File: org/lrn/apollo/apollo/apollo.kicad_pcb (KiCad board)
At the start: 2 copper layers, 47 parts, among them J1 Conn_01x01_Male, J2 Conn_01x01_Male, J3 Conn_01x01_Male, J4 Conn_01x01_Male, Q1 PN2222A, Q2 PN2222A, Q3 PN2222A, Q4 PN2222A, U1 74HC595, U2 5461AS-1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

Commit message: apollo: keyb dbg wip
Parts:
- removed the J1 at (95.0, 106.2)
- removed the J1 at (95.1, 122.2)
- removed the J1 at (90.6, 106.2)
- removed the J1 at (110.9, 103.9)
- moved JA_15 95.9 mm to (111.8, 30.1), turned to 0 degrees
- moved JDS_14 94.8 mm to (141.0, 38.2), turned to 270 degrees
- moved U3 91.8 mm to (119.4, 32.6), turned to 0 degrees
- moved JB_1 91.0 mm to (111.8, 32.6), turned to 0 degrees
- moved JC_2 85.9 mm to (111.8, 35.1), turned to 0 degrees
- moved JST_CP_RCLK_12 85.8 mm to (141.0, 44.0), turned to 0 degrees
- moved JD_3 80.8 mm to (111.8, 37.7), turned to 0 degrees
- moved JSH_CP_SRCLK_11 79.2 mm to (141.0, 49.8), turned to 0 degrees
- moved JE_4 75.7 mm to (111.8, 40.2), turned to 0 degrees
- moved JF_5 70.7 mm to (111.8, 42.7), turned to 0 degrees
- moved JG_6 65.6 mm to (111.8, 45.3), turned to 0 degrees
- moved JH_7 60.5 mm to (111.8, 47.8), turned to 0 degrees
- moved J1 56.1 mm to (183.7, 55.6)
- moved J2 56.1 mm to (166.3, 55.6)
- moved J3 56.1 mm to (172.1, 55.6)
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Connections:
- U4 pad 14: Net-(U4-Pad14) -> Net-(JST_CP_RCLK_12-Pad1)
- U4 pad 15: Net-(U4-Pad15) -> Net-(JSH_CP_SRCLK_11-Pad1)
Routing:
- net Net-(JSH_CP_SRCLK_11-Pad1): track 8.64 -> 21.9 mm
- net Net-(JST_CP_RCLK_12-Pad1): track 8.66 -> 21.8 mm
- net VCC: track 56.8 -> 52.8 mm

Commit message: apollo: pcb additions
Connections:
- U4 pad 13: Net-(U4-Pad13) -> Net-(JDS_14-Pad1)
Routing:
- net Net-(JDS_14-Pad1): track 8.59 -> 26.6 mm
- net GND: track 248.6 -> 243.8 mm
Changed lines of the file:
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@@
     (thickness 1.6)
     (drawings 0)
-    (tracks 254)
+    (tracks 259)
     (zones 0)
     (modules 43)
-    (nets 63)
+    (nets 62)
   )
   (page A4)
@@
   (net 50 "Net-(U4-Pad12)")
   (net 51 "Net-(U4-Pad3)")
-  (net 52 "Net-(U4-Pad13)")
-  (net 53 "Net-(U4-Pad4)")
-  (net 54 "Net-(U4-Pad5)")
-  (net 55 "Net-(U4-Pad6)")
-  (net 56 "Net-(U4-Pad9)")
-  (net 57 "Net-(U4-Pad10)")
-  (net 58 "Net-(U4-Pad20)")
-  (net 59 "Net-(U4-Pad21)")
-  (net 60 "Net-(J_MOSI_1-Pad1)")
-  (net 61 "Net-(J_MISO_1-Pad1)")
-  (net 62 "Net-(J_SCK_1-Pad1)")
+  (net 52 "Net-(U4-Pad4)")
+  (net 53 "Net-(U4-Pad5)")
+  (net 54 "Net-(U4-Pad6)")
+  (net 55 "Net-(U4-Pad9)")
+  (net 56 "Net-(U4-Pad10)")
+  (net 57 "Net-(U4-Pad20)")
+  (net 58 "Net-(U4-Pad21)")
+  (net 59 "Net-(J_MOSI_1-Pad1)")
+  (net 60 "Net-(J_MISO_1-Pad1)")
+  (net 61 "Net-(J_SCK_1-Pad1)")
   (net_class Default "This is the default net class."
     (clearance 0.8)
@@
     (add_net "Net-(U4-Pad11)")
     (add_net "Net-(U4-Pad12)")
-    (add_net "Net-(U4-Pad13)")
     (add_net "Net-(U4-Pad2)")
     (add_net "Net-(U4-Pad20)")
@@
       (net 51 "Net-(U4-Pad3)"))
     (pad 17 thru_hole oval (at 7.62 27.94 270) (size 3 1.6) (drill 0.8) (layers *.Cu *.Mask)
-      (net 60 "Net-(J_MOSI_1-Pad1)"))
+      (net 59 "Net-(J_MOSI_1-Pad1)"))
     (pad 4 thru_hole oval (at 0 7.62 270) (size 3 1.6) (drill 0.8) (layers *.Cu *.Mask)
-      (net 53 "Net-(U4-Pad4)"))
+      (net 52 "Net-(U4-Pad4)"))
     (pad 18 thru_hole oval (at 7.62 25.4 270) (size 3 1.6) (drill 0.8) (layers *.Cu *.Mask)
-      (net 61 "Net-(J_MISO_1-Pad1)"))
+      (net 60 "Net-(J_MISO_1-Pad1)"))
     (pad 5 thru_hole oval (at 0 10.16 270) (size 3 1.6) (drill 0.8) (layers *.Cu *.Mask)
-      (net 54 "Net-(U4-Pad5)"))
+      (net 53 "Net-(U4-Pad5)"))
     (pad 19 thru_hole oval (at 7.62 22.86 270) (size 3 1.6) (drill 0.8) (layers *.Cu *.Mask)
-      (net 62 "Net-(J_SCK_1-Pad1)"))
+      (net 61 "Net-(J_SCK_1-Pad1)"))
     (pad 6 thru_hole oval (at 0 12.7 270) (size 3 1.6) (drill 0.8) (layers *.Cu *.Mask)
-      (net 55 "Net-(U4-Pad6)"))
+      (net 54 "Net-(U4-Pad6)"))
     (pad 20 thru_hole oval (at 7.62 20.32 270) (size 3 1.6) (drill 0.8) (layers *.Cu *.Mask)
-      (net 58 "Net-(U4-Pad20)"))
+      (net 57 "Net-(U4-Pad20)"))
     (pad 7 thru_hole oval (at 0 15.24 270) (size 3 1.6) (drill 0.8) (layers *.Cu *.Mask)
       (net 34 VCC))
     (pad 21 thru_hole oval (at 7.62 17.78 270) (size 3 1.6) (drill 0.8) (layers *.Cu *.Mask)
-      (net 59 "Net-(U4-Pad21)"))
+      (net 58 "Net-(U4-Pad21)"))
     (pad 8 thru_hole oval (at 0 17.78 270) (size 3 1.6) (drill 0.8) (layers *.Cu *.Mask)
       (net 33 GND))
@@
       (net 33 GND))
     (pad 9 thru_hole oval (at 0 20.32 270) (size 3 1.6) (drill 0.8) (layers *.Cu *.Mask)
-      (net 56 "Net-(U4-Pad9)"))
+      (net 55 "Net-(U4-Pad9)"))
     (pad 23 thru_hole oval (at 7.62 12.7 270) (size 3 1.6) (drill 0.8) (layers *.Cu *.Mask)
       (net 3 "Net-(J2-Pad1)"))
     (pad 10 thru_hole oval (at 0 22.86 270) (size 3 1.6) (drill 0.8) (layers *.Cu *.Mask)
-      (net 57 "Net-(U4-Pad10)"))
+      (net 56 "Net-(U4-Pad10)"))
     (pad 24 thru_hole oval (at 7.62 10.16 270) (size 3 1.6) (drill 0.8) (layers *.Cu *.Mask)
       (net 4 "Net-(J3-Pad1)"))
@@
       (net 2 "Net-(J1-Pad1)"))
     (pad 13 thru_hole oval (at 0 30.48 270) (size 3 1.6) (drill 0.8) (layers *.Cu *.Mask)
-      (net 52 "Net-(U4-Pad13)"))
+      (net 39 "Net-(JDS_14-Pad1)"))
     (pad 27 thru_hole oval (at 7.62 2.54 270) (size 3 1.6) (drill 0.8) (layers *.Cu *.Mask)
       (net 8 "Net-(J_SER1-Pad1)"))
@@
     )
     (pad 1 thru_hole oval (at 0 0 90) (size 3 1.6) (drill 0.7) (layers *.Cu *.Mask)
-      (net 61 "Net-(J_MISO_1-Pad1)"))
+      (net 60 "Net-(J_MISO_1-Pad1)"))
     (model ${KISYS3DMOD}/Connector_Pin.3dshapes/Pin_D0.7mm_L6.5mm_W1.8mm_FlatFork.wrl
       (at (xyz 0 0 0))
@@
     (fp_line (start 1.35 1.2) (end -1.4 1.2) (layer F.CrtYd) (width 0.05))
     (pad 1 thru_hole oval (at 0 0 90) (size 3 1.6) (drill 0.7) (layers *.Cu *.Mask)
-      (net 60 "Net-(J_MOSI_1-Pad1)"))
+      (net 59 "Net-(J_MOSI_1-Pad1)"))
     (model ${KISYS3DMOD}/Connector_Pin.3dshapes/Pin_D0.7mm_L6.5mm_W1.8mm_FlatFork.wrl
       (at (xyz 0 0 0))
@@
     (fp_line (start 1.35 1.2) (end -1.4 1.2) (layer F.CrtYd) (width 0.05))
     (pad 1 thru_hole oval (at 0 0 90) (size 3 1.6) (drill 0.7) (layers *.Cu *.Mask)
-      (net 62 "Net-(J_SCK_1-Pad1)"))
+      (net 61 "Net-(J_SCK_1-Pad1)"))
     (model ${KISYS3DMOD}/Connector_Pin.3dshapes/Pin_D0.7mm_L6.5mm_W1.8mm_FlatFork.wrl
       (at (xyz 0 0 0))
@@
   (segment (start 123.33732 49.4792) (end 122.463359 50.353161) (width 1) (layer B.Cu) (net 33))
   (segment (start 119.447841 50.353161) (end 119.447841 50.366399) (width 1) (layer B.Cu) (net 33))
-  (segment (start 119.447841 50.366399) (end 117.71122 52.10302) (width 1) (layer B.Cu) (net 33))
-  (segment (start 117.71122 52.10302) (end 115.33886 52.10302) (width 1) (layer B.Cu) (net 33))
   (segment (start 157.05836 125.0788) (end 139.9632 125.0788) (width 1) (layer B.Cu) (net 33))
   (segment (start 163.8808 71.5518) (end 163.8808 70.231) (width 1) (layer B.Cu) (net 33))
@@
   (segment (start 135.661199 37.653161) (end 135.6614 37.65296) (width 1) (layer B.Cu) (net 39))
   (segment (start 127.067841 37.653161) (end 135.661199 37.653161) (width 1) (layer B.Cu) (net 39))
+  (segment (start 148.5138 36.2604) (end 146.5434 34.29) (width 1) (layer B.Cu) (net 39))
+  (segment (start 148.5138 38.7604) (end 148.5138 36.2604) (width 1) (layer B.Cu) (net 39))
+  (segment (start 144.9264 34.29) (end 141.0208 38.1956) (width 1) (layer B.Cu) (net 39))
+  (segment (start 146.5434 34.29) (end 144.9264 34.29) (width 1) (layer B.Cu) (net 39))
+  (segment (start 135.661199 37.653161) (end 136.651799 37.653161) (width 1) (layer B.Cu) (net 39))
+  (segment (start 137.194238 38.1956) (end 141.0208 38.1956) (width 1) (layer B.Cu) (net 39))
+  (segment (start 136.651799 37.653161) (end 137.194238 38.1956) (width 1) (layer B.Cu) (net 39))
   (segment (start 111.856319 40.193161) (end 111.81588 40.2336) (width 1) (layer B.Cu) (net 40))
   (segment (start 119.447841 40.193161) (end 111.856319 40.193161) (width 1) (layer B.Cu) (net 40))
@@
   (segment (start 141.0208 43.7134) (end 145.9738 38.7604) (width 1) (layer B.Cu) (net 45))
   (segment (start 141.0208 44.0122) (end 141.0208 43.7134) (width 1) (layer B.Cu) (net 45))
-  (segment (start 151.0538 46.3804) (end 151.0538 52.0058) (width 1) (layer B.Cu) (net 60))
-  (segment (start 153.5938 51.9804) (end 153.6192 52.0058) (width 1) (layer B.Cu) (net 61))
-  (segment (start 153.5938 46.3804) (end 153.5938 51.9804) (width 1) (layer B.Cu) (net 61))
-  (segment (start 156.1338 46.3804) (end 156.1338 52.0058) (width 1) (layer B.Cu) (net 62))
+  (segment (start 151.0538 46.3804) (end 151.0538 52.0058) (width 1) (layer B.Cu) (net 59))
+  (segment (start 153.5938 51.9804) (end 153.6192 52.0058) (width 1) (layer B.Cu) (net 60))
+  (segment (start 153.5938 46.3804) (end 153.5938 51.9804) (width 1) (layer B.Cu) (net 60))
+  (segment (start 156.1338 46.3804) (end 156.1338 52.0058) (width 1) (layer B.Cu) (net 61))
 )

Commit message: apollo: before keyb scan
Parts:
- moved JH_7 8.39 mm to (119.3, 51.5)
- moved U3 8.39 mm to (127.0, 36.3)
- moved JA_15 8.39 mm to (119.3, 33.8)
- moved JC_2 8.39 mm to (119.3, 38.8)
- moved JD_3 8.39 mm to (119.3, 41.4)
- moved JF_5 8.39 mm to (119.3, 46.5)
- moved JG_6 8.39 mm to (119.4, 49.0)
- moved JB_1 8.39 mm to (119.3, 36.3)
- moved JE_4 8.39 mm to (119.3, 44.0)
- renumbered J_CLR1 to J_D_CLOCK_1, J_SER1 to J_D_DATA_1, J_CLK1 to J_D_LATCH_1, JSH_CP_SRCLK_11 to J_K_CLOCK_1, JDS_14 to J_K_DATA_1, JST_CP_RCLK_12 to J_K_LATCH_1
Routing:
- net VCC: track 52.8 -> 82.1 mm, vias 2 -> 0
- net Net-(JA_15-Pad1): track 19.2 -> 0.00 mm
- net GND: track 243.8 -> 227.4 mm
- net Net-(J_K_CLOCK_1-Pad1): track 21.9 -> 12.5 mm
- net Net-(J_K_DATA_1-Pad1): track 26.6 -> 18.3 mm
- net Net-(J_K_LATCH_1-Pad1): track 21.8 -> 14.3 mm
- net Net-(J_D_LATCH_1-Pad1): track 153.2 -> 150.7 mm

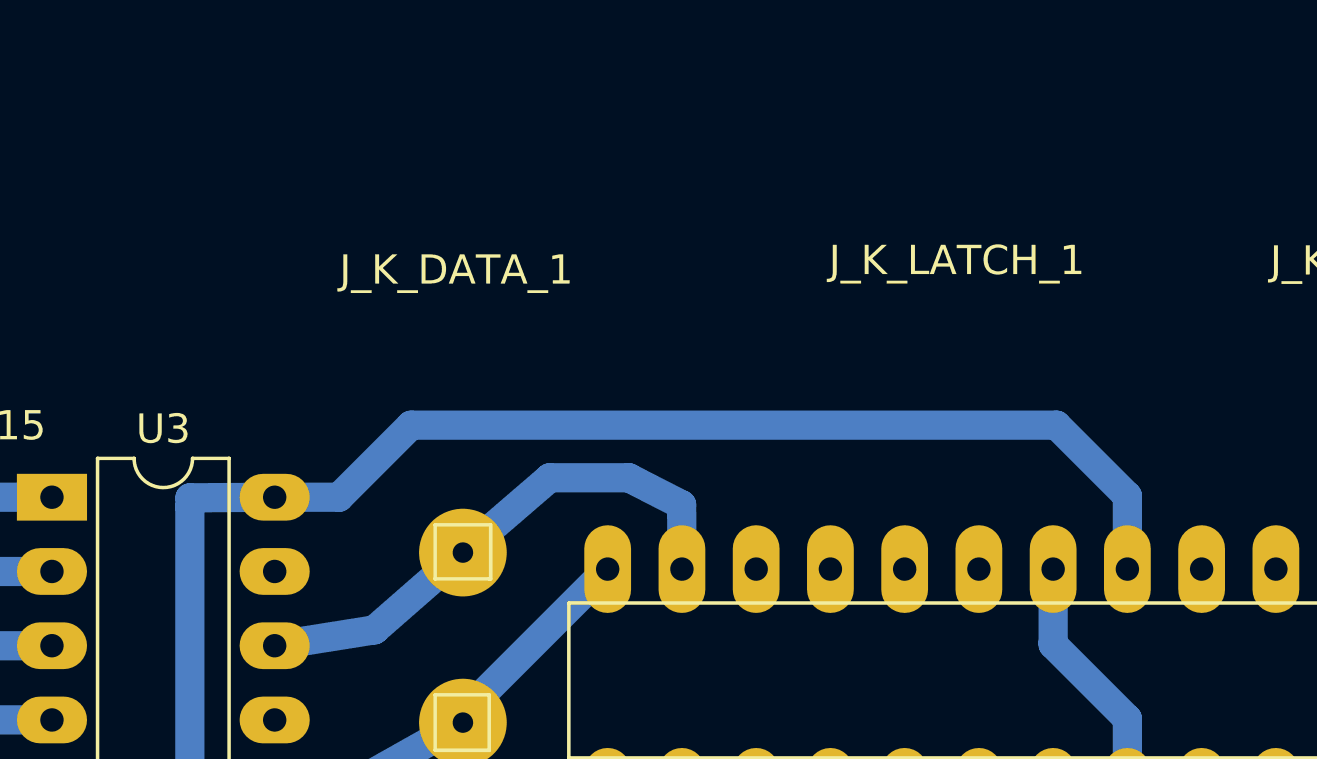
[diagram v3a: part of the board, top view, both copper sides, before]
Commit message: apollo: beep schematic
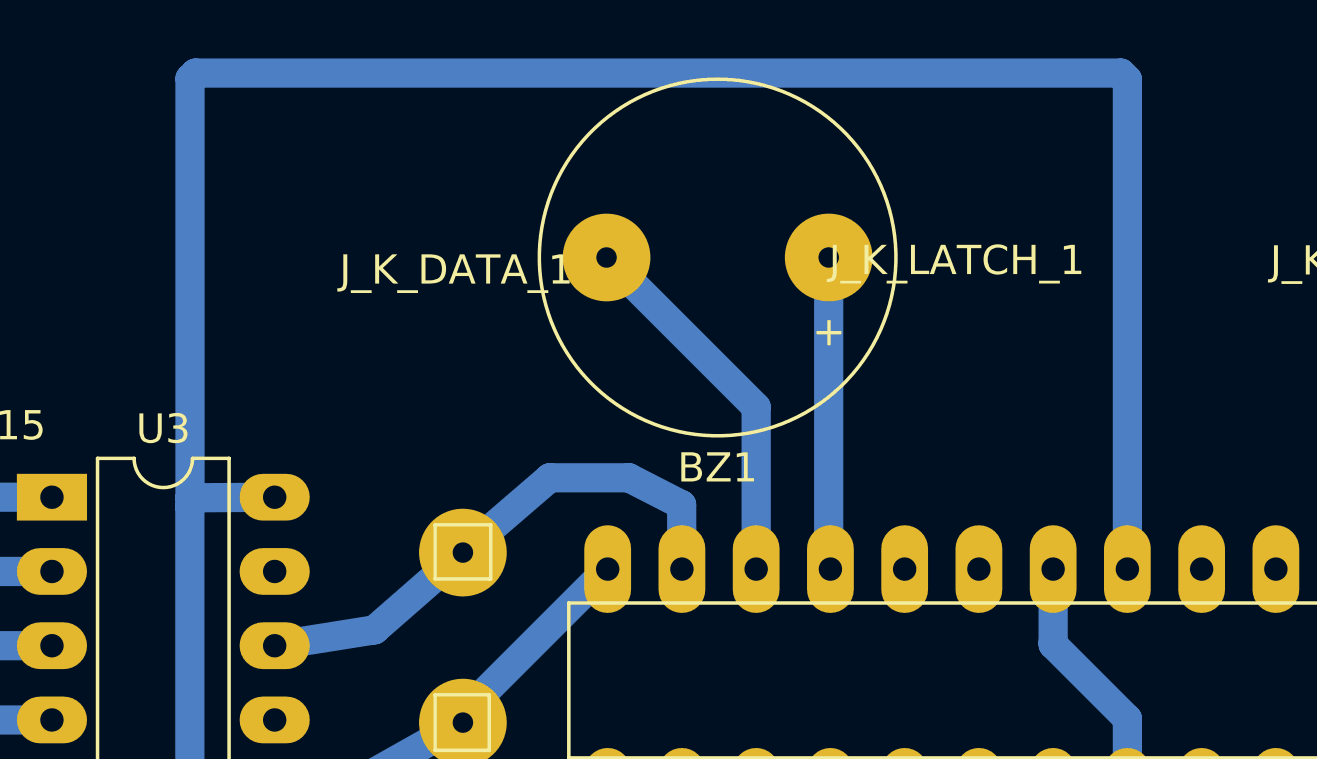
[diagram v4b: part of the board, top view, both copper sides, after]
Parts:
- added BZ1: Buzzer, Buzzer_Beeper:Buzzer_12x9.5RM7.6, F.Cu at (153.5, 28.1)
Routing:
- net VCC: track 82.1 -> 111.7 mm
- net Net-(BZ1-Pad2): track 0.00 -> 12.8 mm
- net Net-(BZ1-Pad1): track 0.00 -> 10.7 mm

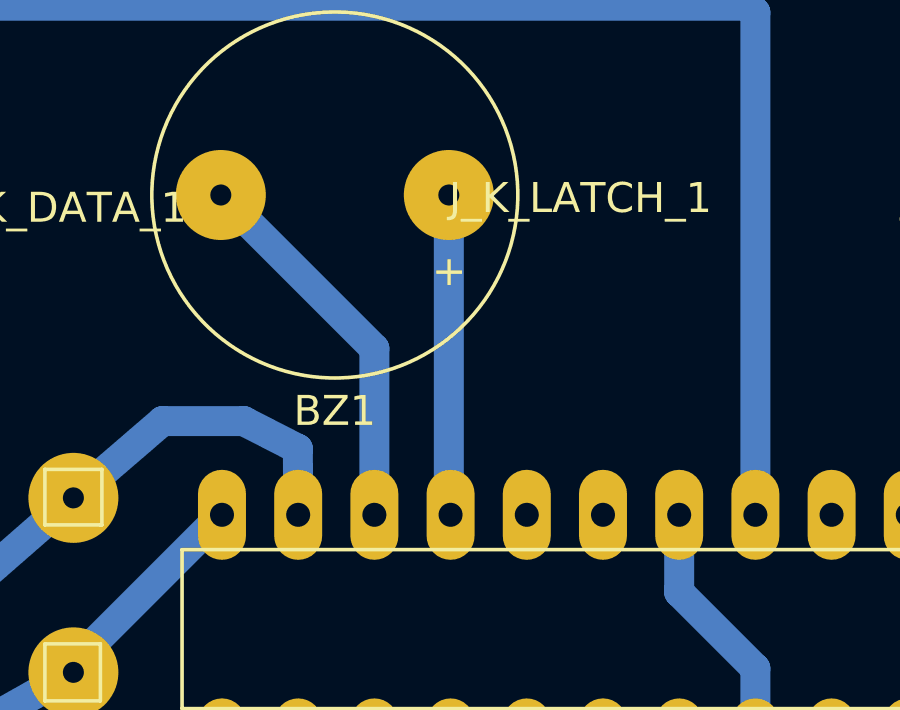
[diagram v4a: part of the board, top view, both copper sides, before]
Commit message: apollo: switch buzzer to Timer0-CTC for use only one MCU pin
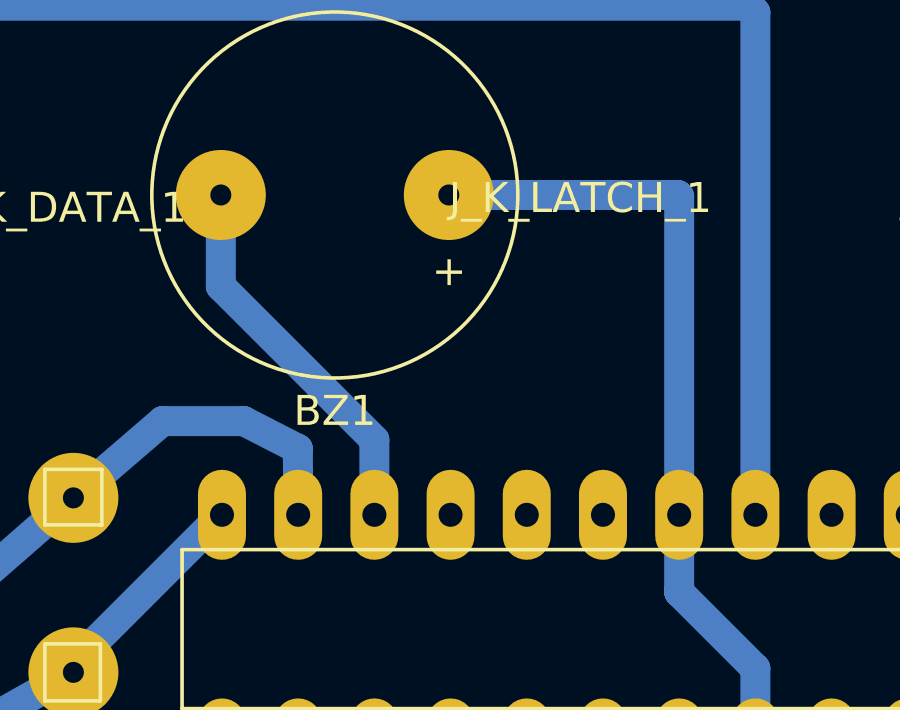
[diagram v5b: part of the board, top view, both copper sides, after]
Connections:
- BZ1 pad 1: Net-(BZ1-Pad1) -> GND
- U4 pad 11: Net-(BZ1-Pad1) -> Net-(U4-Pad11)
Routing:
- net GND: track 227.4 -> 245.8 mm
- net Net-(BZ1-Pad1): track 10.7 -> 0.00 mm
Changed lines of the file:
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@@
     (thickness 1.6)
     (drawings 0)
-    (tracks 246)
+    (tracks 248)
     (zones 0)
     (modules 44)
@@
   (net 58 "Net-(J_K_DATA_1-Pad1)")
   (net 59 "Net-(J_K_LATCH_1-Pad1)")
-  (net 60 "Net-(BZ1-Pad1)")
-  (net 61 "Net-(BZ1-Pad2)")
+  (net 60 "Net-(BZ1-Pad2)")
+  (net 61 "Net-(U4-Pad11)")
   (net_class Default "This is the default net class."
     (clearance 0.8)
@@
     (diff_pair_gap 0.8)
     (add_net GND)
-    (add_net "Net-(BZ1-Pad1)")
     (add_net "Net-(BZ1-Pad2)")
     (add_net "Net-(J1-Pad1)")
@@
     (add_net "Net-(U4-Pad1)")
     (add_net "Net-(U4-Pad10)")
+    (add_net "Net-(U4-Pad11)")
     (add_net "Net-(U4-Pad2)")
     (add_net "Net-(U4-Pad20)")
@@
       (net 4 "Net-(J3-Pad1)"))
     (pad 11 thru_hole oval (at 0 25.4 270) (size 3 1.6) (drill 0.8) (layers *.Cu *.Mask)
-      (net 60 "Net-(BZ1-Pad1)"))
+      (net 61 "Net-(U4-Pad11)"))
     (pad 25 thru_hole oval (at 7.62 7.62 270) (size 3 1.6) (drill 0.8) (layers *.Cu *.Mask)
       (net 5 "Net-(J4-Pad1)"))
     (pad 12 thru_hole oval (at 0 27.94 270) (size 3 1.6) (drill 0.8) (layers *.Cu *.Mask)
-      (net 61 "Net-(BZ1-Pad2)"))
+      (net 60 "Net-(BZ1-Pad2)"))
     (pad 26 thru_hole oval (at 7.62 5.08 270) (size 3 1.6) (drill 0.8) (layers *.Cu *.Mask)
       (net 2 "Net-(J1-Pad1)"))
@@
     (fp_circle (center 3.8 0) (end 9.9 0) (layer F.SilkS) (width 0.12))
     (pad 1 thru_hole circle (at 0 0 180) (size 3 3) (drill 0.7) (layers *.Cu *.Mask)
-      (net 60 "Net-(BZ1-Pad1)"))
+      (net 30 GND))
     (pad 2 thru_hole circle (at 7.6 0 180) (size 3 3) (drill 0.7) (layers *.Cu *.Mask)
-      (net 61 "Net-(BZ1-Pad2)"))
+      (net 60 "Net-(BZ1-Pad2)"))
     (model ${KISYS3DMOD}/Buzzer_Beeper.3dshapes/Buzzer_12x9.5RM7.6.wrl
       (at (xyz 0 0 0))
@@
   (segment (start 161.2138 41.3404) (end 161.2138 41.2604) (width 1) (layer B.Cu) (net 30))
   (segment (start 161.2138 41.2604) (end 161.2138 38.7604) (width 1) (layer B.Cu) (net 30))
+  (segment (start 153.53538 28.10002) (end 161.17316 28.10002) (width 1) (layer B.Cu) (net 30))
+  (segment (start 161.2138 28.14066) (end 161.2138 38.7604) (width 1) (layer B.Cu) (net 30))
+  (segment (start 161.17316 28.10002) (end 161.2138 28.14066) (width 1) (layer B.Cu) (net 30))
   (segment (start 159.6136 129.5146) (end 159.59836 129.52984) (width 1) (layer B.Cu) (net 31))
   (segment (start 174.15416 129.5146) (end 159.6136 129.5146) (width 1) (layer B.Cu) (net 31))
@@
   (segment (start 141.0208 43.7134) (end 145.9738 38.7604) (width 1) (layer B.Cu) (net 59))
   (segment (start 141.0208 44.0122) (end 141.0208 43.7134) (width 1) (layer B.Cu) (net 59))
-  (segment (start 153.53538 38.70198) (end 153.5938 38.7604) (width 1) (layer B.Cu) (net 60))
-  (segment (start 153.53538 28.10002) (end 153.53538 38.70198) (width 1) (layer B.Cu) (net 60))
-  (segment (start 151.0538 33.21844) (end 145.93538 28.10002) (width 1) (layer B.Cu) (net 61))
-  (segment (start 151.0538 38.7604) (end 151.0538 33.21844) (width 1) (layer B.Cu) (net 61))
+  (segment (start 145.93538 31.14198) (end 145.93538 28.10002) (width 1) (layer B.Cu) (net 60))
+  (segment (start 151.0538 36.2604) (end 145.93538 31.14198) (width 1) (layer B.Cu) (net 60))
+  (segment (start 151.0538 38.7604) (end 151.0538 36.2604) (width 1) (layer B.Cu) (net 60))
 )
